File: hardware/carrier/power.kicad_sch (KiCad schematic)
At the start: 42 parts, among them J1 USB4235, J2 BATTERY, Q1 DMG2305UX-7, SW1 JS102011SAQN, U1 BQ25185DLHR, U10 MAX17048G+T10, U3 TPS62840DLCR, U4 TPS22917DBV

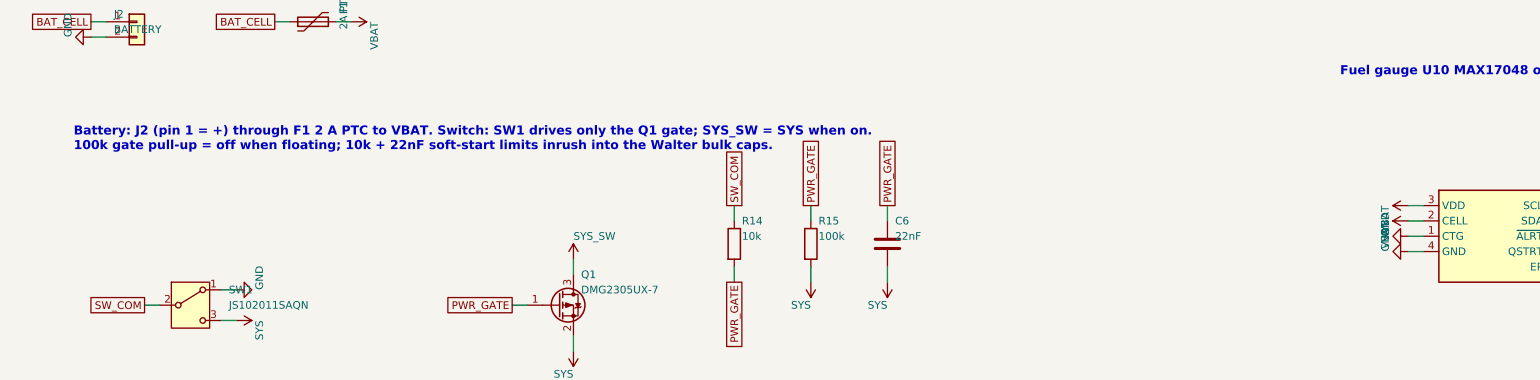
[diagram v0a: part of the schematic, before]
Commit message: hardware/carrier: front light is the GDEY029T94-FL03 (6-pin flex -> FH34SRJ-6S on the panel board, anode/cathode over a 10-way SH cable, 33R 1206 + Q4 PWM drive replaces the NSI45020), front-light button SW2 on IO4 (FL_BTN), low-profile pass (FH34SRJ 1.0 mm ZIFs, 2 x 100uF 0805 instead of the 2.5 mm 1210, part-height table), sleep-current audit (Q1 gate pull-up 100k -> 2.2M: 38 -> 1.9 uA; SN74LVC2G126 moved to the bus-powered BRG_VDD rail: 0 on battery; table in the README), TPS62840 has no fixed-3.3 V variant (README). Custom FH34SRJ footprints from the Hirose catalog; LCSC numbers via the JLCPCB parts API. Both boards re-placed and re-routed: 0 unconnected, 0 clearance/courtyard errors, silk notes only; ERC 0/0; exports refreshed (owner, 17 Oct 2026)
Co-Authored-By: Claude Fable 5.1 <noreply@anthropic.com>
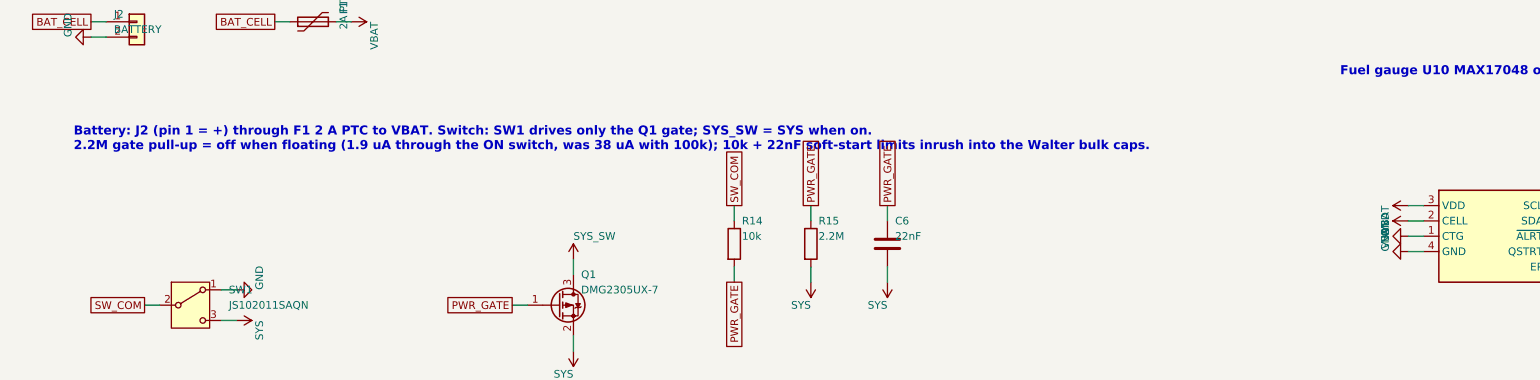
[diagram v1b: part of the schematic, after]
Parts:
- R15: value 100k -> 2.2M; LCSC C25803 -> C22938; MPN 0603WAF1003T5E -> 0603WAF2204T5E; Note (none) -> sleep current: 2.2M, not 100k (SW1 ON pulls it to GND throu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
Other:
- note added: "Battery: J2 (pin 1 = +) through F1 2 A PTC to VBAT. Switch: SW1 drives only the Q1 gate; SYS_SW = SYS when on. 2.2M gate pull-up = off when floating (1.9 uA through the ON switch, was 38 uA with 100k); 10k + 22nF soft-start limits inrush into the Walter bulk caps."
- note removed: "Battery: J2 (pin 1 = +) through F1 2 A PTC to VBAT. Switch: SW1 drives only the Q1 gate; SYS_SW = SYS when on. 100k gate pull-up = off when floating; 10k + 22nF soft-start limits inrush into the Walter bulk caps."
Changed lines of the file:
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@@
 		)
 	)
-	(text "Battery: J2 (pin 1 = +) through F1 2 A PTC to VBAT. Switch: SW1 drives only the Q1 gate; SYS_SW = SYS when on.\n100k gate pull-up = off when floating; 10k + 22nF soft-start limits inrush into the Walter bulk caps."
+	(text "Battery: J2 (pin 1 = +) through F1 2 A PTC to VBAT. Switch: SW1 drives only the Q1 gate; SYS_SW = SYS when on.\n2.2M gate pull-up = off when floating (1.9 uA through the ON switch, was 38 uA with 100k); 10k + 22nF soft-start limits inrush into the Walter bulk caps."
 		(exclude_from_sim no)
 		(at 20 232 0)
@@
 			)
 		)
-		(property "Value" "100k"
+		(property "Value" "2.2M"
 			(at 143.51 250.19 0)
 			(effects
@@
 			)
 		)
-		(property "MPN" "0603WAF1003T5E"
+		(property "MPN" "0603WAF2204T5E"
 			(at 142.24 266.7 0)
 			(hide yes)
@@
 			)
 		)
-		(property "LCSC" "C25803"
+		(property "LCSC" "C22938"
 			(at 142.24 269.24 0)
 			(hide yes)
@@
 			(hide yes)
 			(effects
+				(font
+					(size 1.27 1.27)
+				)
+			)
+		)
+		(property "Note" "sleep current: 2.2M, not 100k (SW1 ON pulls it to GND through 10k)"
+			(at 142.24 274.32 0)
+			(hide yes)
+			(effects
